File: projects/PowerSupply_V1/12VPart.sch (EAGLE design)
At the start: 26 parts, among them IC1 LM2596T, IC2 LM2596T, X1 IN, X2 OUT

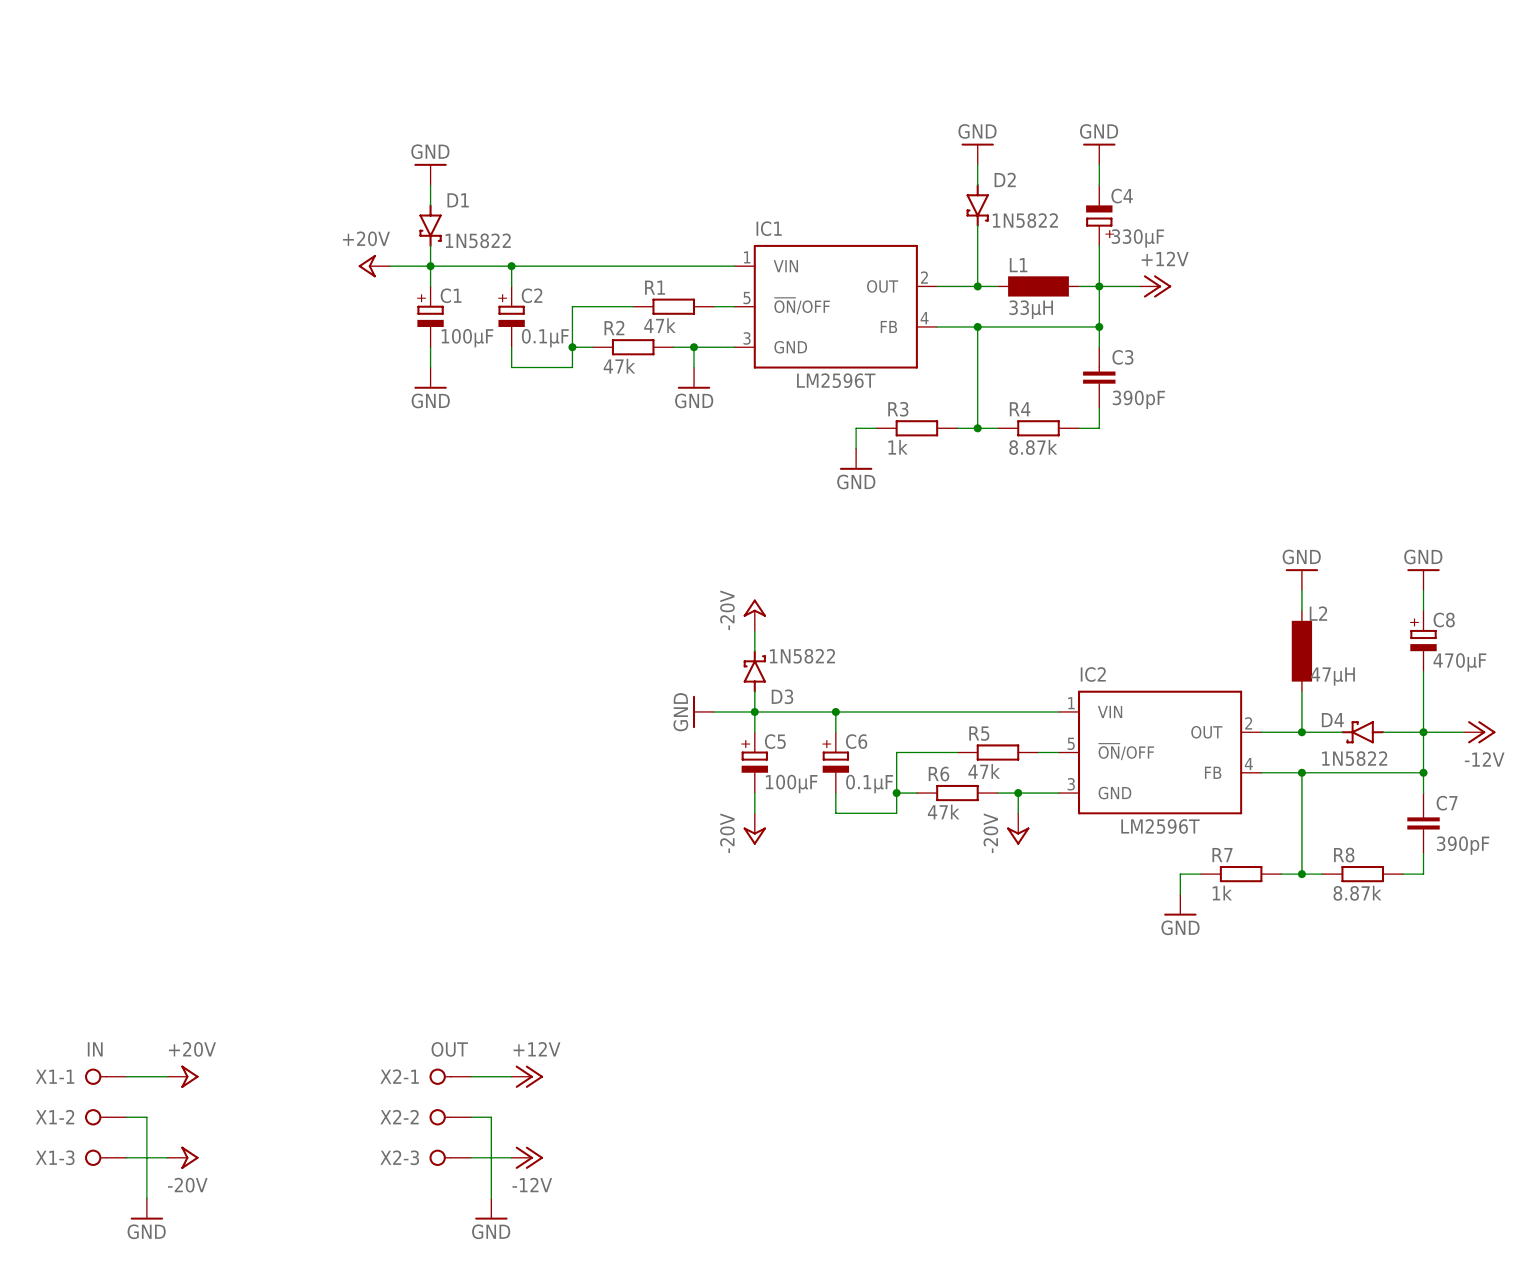
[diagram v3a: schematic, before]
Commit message: refactor(all): schematics and routing changed
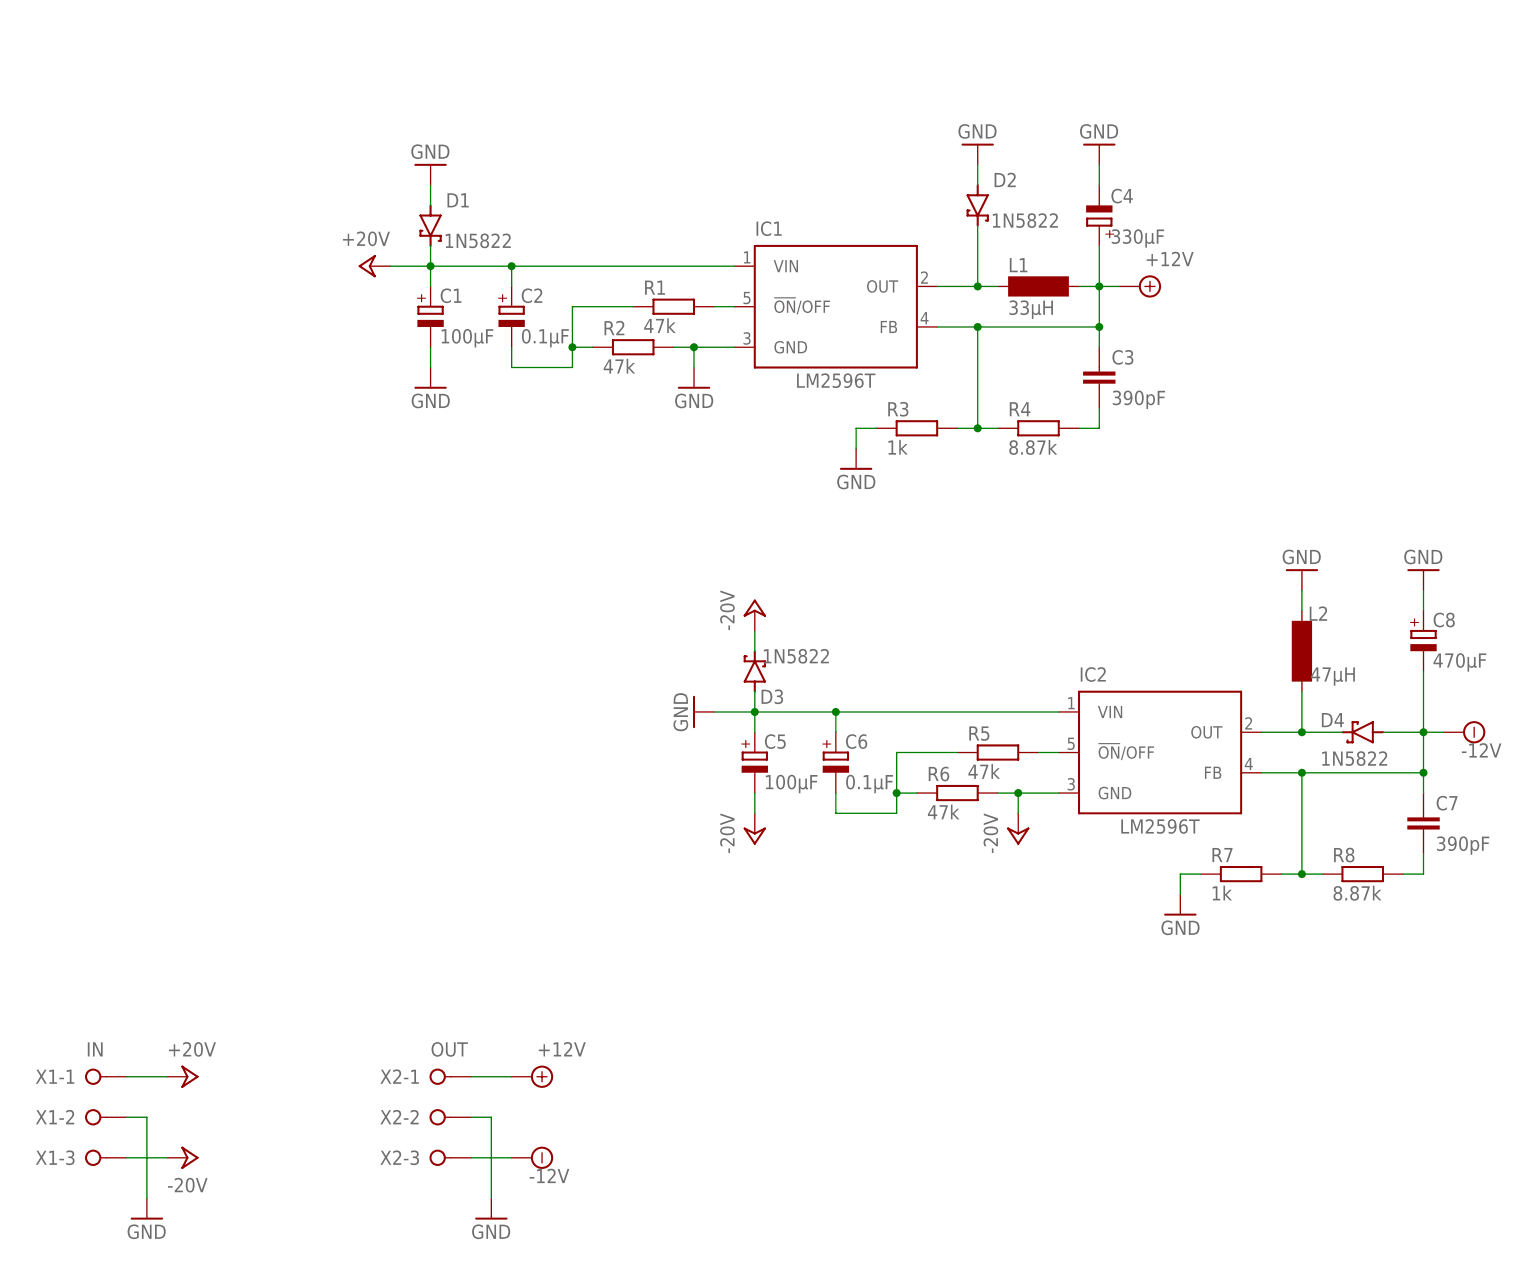
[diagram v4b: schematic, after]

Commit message: feat: 12VPart refactored
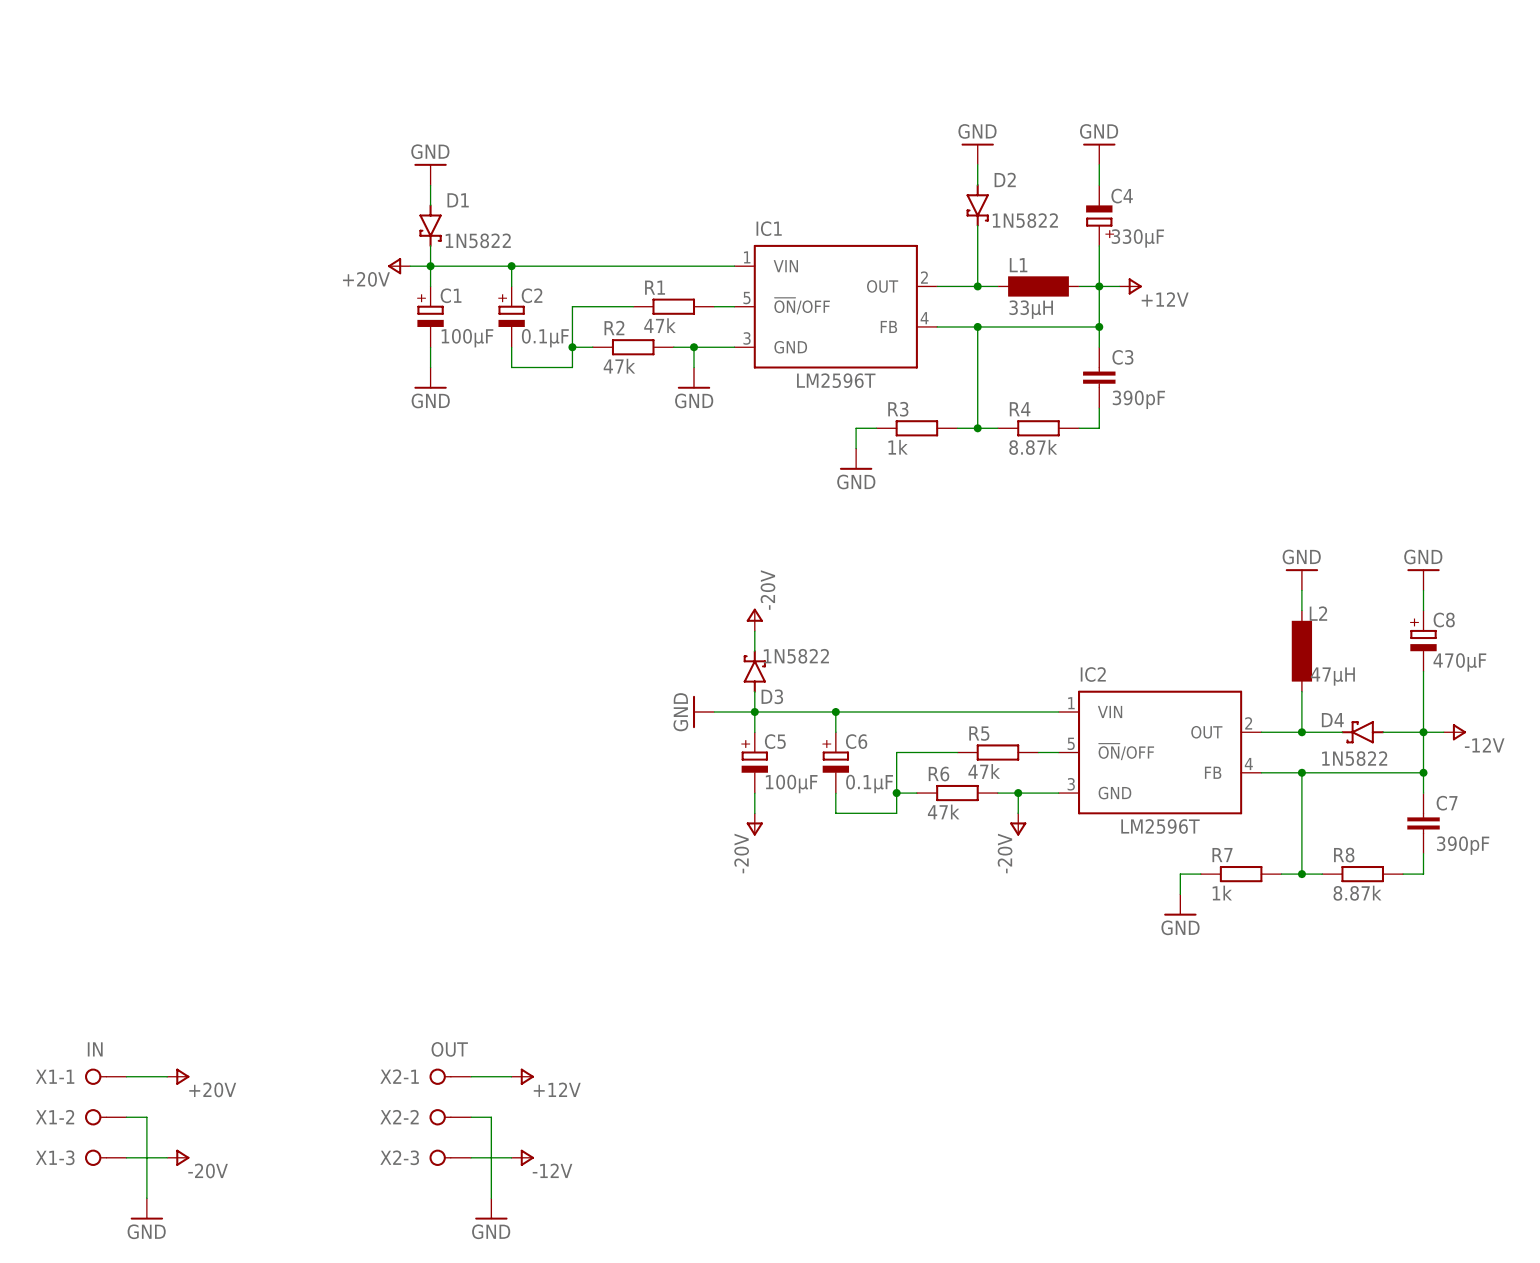
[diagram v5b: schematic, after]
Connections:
- net +24V renamed +20V
- net -24V renamed -20V
